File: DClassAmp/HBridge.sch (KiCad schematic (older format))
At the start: 27 parts

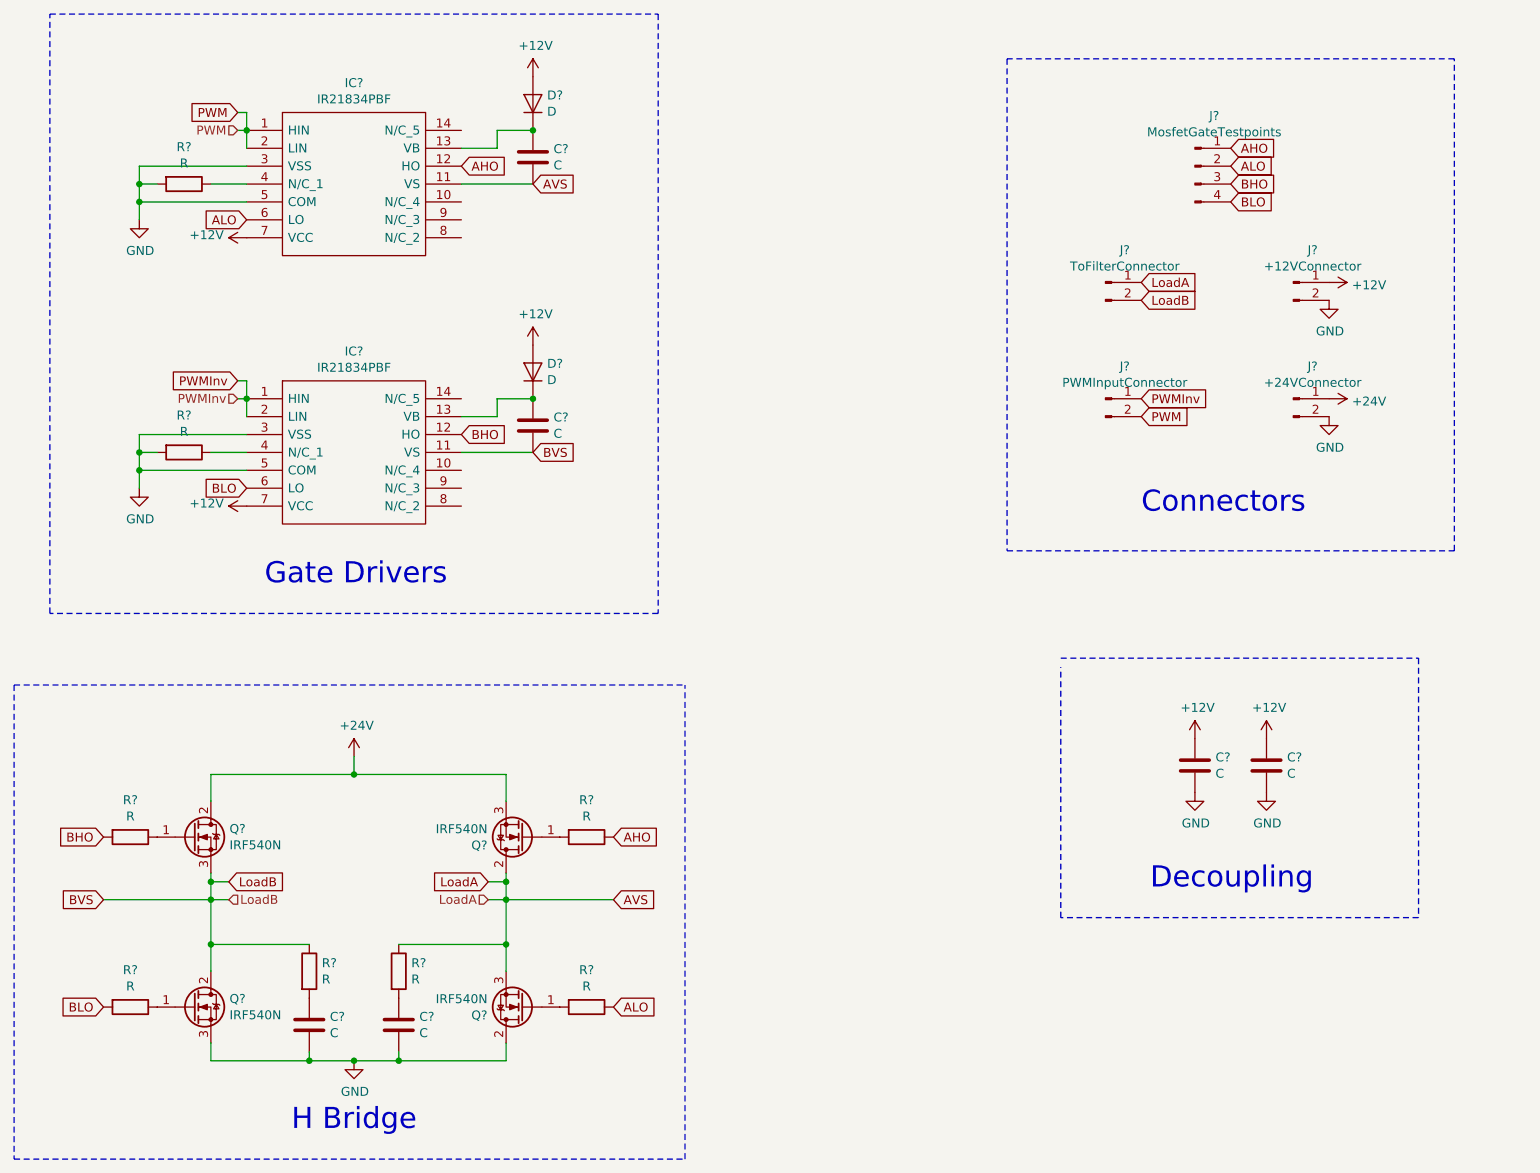
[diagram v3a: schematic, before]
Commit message: Added h bridge pcb
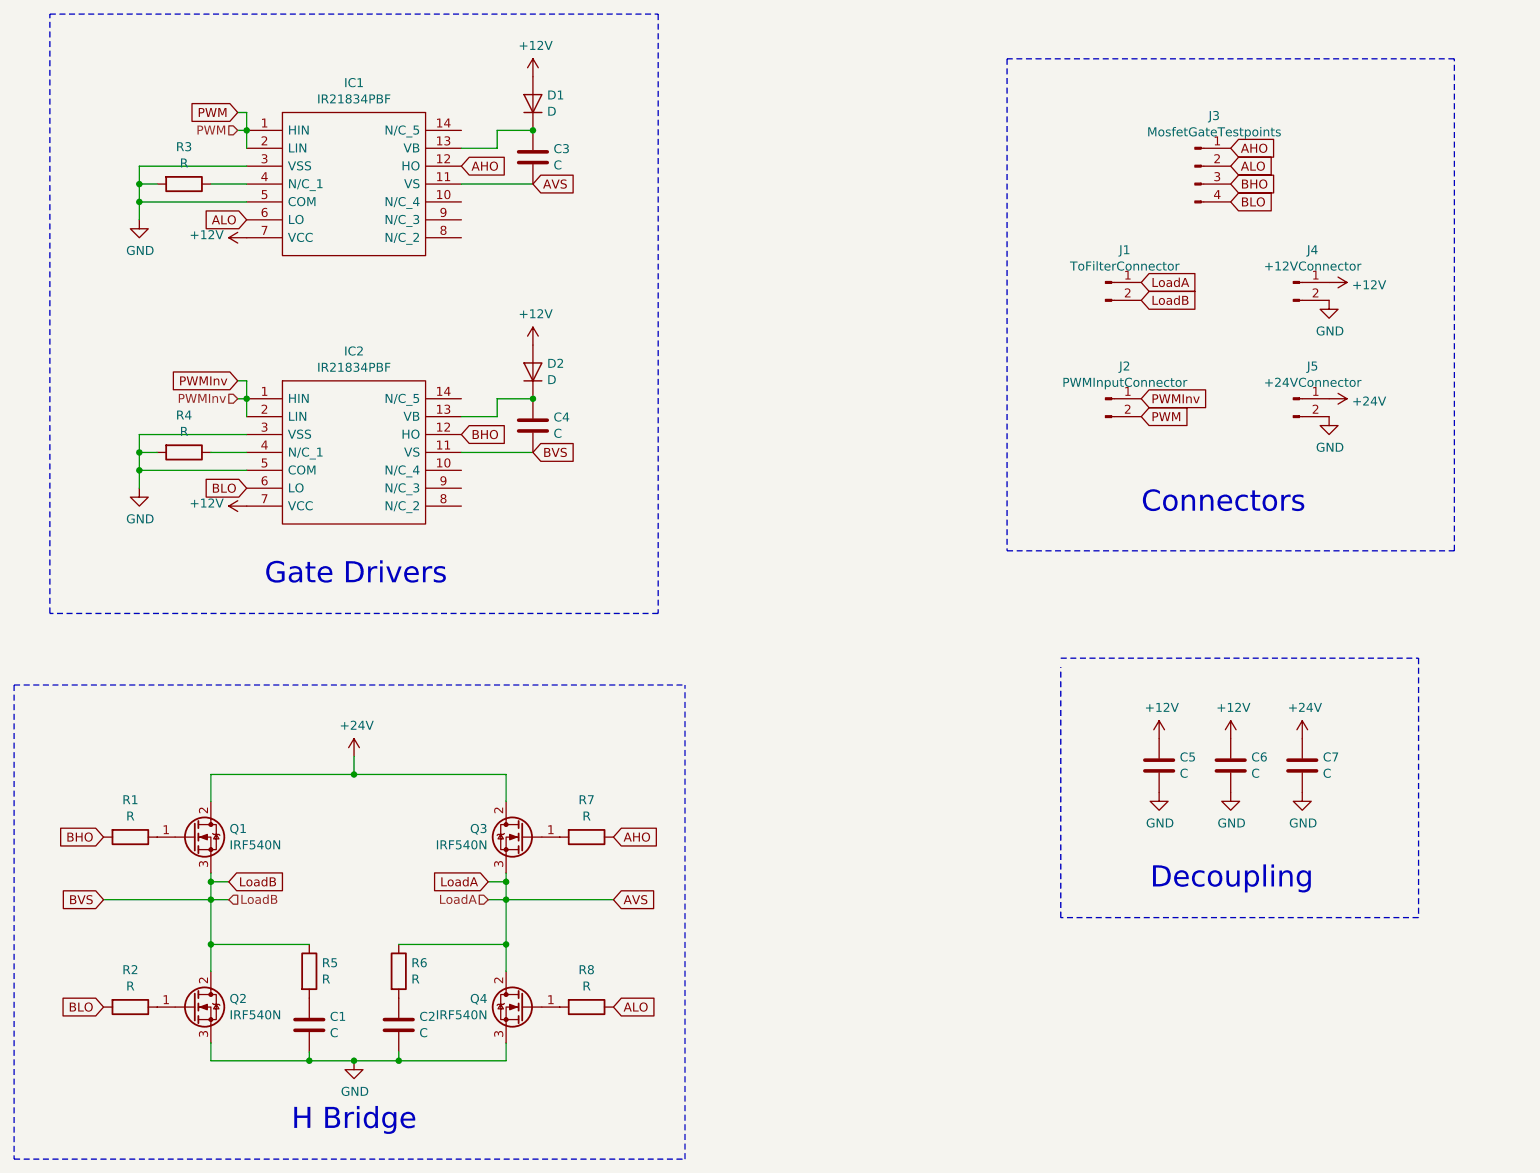
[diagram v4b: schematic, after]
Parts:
- added C7: C, Capacitor_THT:CP_Radial_D12.5mm_P5.00mm, symbol Device:C
- C1, C2, C3, C4, C5, C6: renamed from C?; footprint (none) -> Capacitor_THT:CP_Radial_D12.5mm_P5.00mm
- D1, D2: renamed from D?; footprint (none) -> Diode_THT:D_DO-15_P12.70mm_Horizontal
- IC1, IC2: renamed from IC?; footprint DIP762W56P254L1930H533Q14N -> Package_DIP:DIP-14_W7.62mm
- J1, J2, J4, J5: renamed from J?; footprint (none) -> Connector_PinHeader_2.00mm:PinHeader_1x02_P2.00mm_Vertical
- J3: renamed from J?; footprint (none) -> Connector_PinHeader_2.00mm:PinHeader_1x04_P2.00mm_Vertical
- R1, R2, R3, R4, R5, R6, R7, R8: renamed from R?; footprint (none) -> Resistor_THT:R_Axial_DIN0309_L9.0mm_D3.2mm_P15.24mm_Horizontal
- gave numbers to parts that had none: 4
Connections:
- net +24V: now also Q3.2 (D), C7.1; no longer Q3.3 (S)
- net AVS: now also Q3.3 (S), Q4.2 (D); no longer Q3.2 (D), Q4.3 (S)
- net GND: now also Q4.3 (S), C7.2; no longer Q4.2 (D)
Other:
- moved on the sheet: C5, C6
